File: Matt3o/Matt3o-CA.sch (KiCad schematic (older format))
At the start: 152 parts, among them IC1 ATMEGA32U4, K1 AVR_ICSP, P1 CONN_4, P2 CONN_4, SW1 TILDE, SW10 FN, SW11 2, SW12 W, SW13 S, SW14 X, SW15 ALT, SW16 3, SW17 E, SW18 D, SW19 C, SW2 TAB, SW20 4, SW21 R, SW22 F, SW23 V, SW24 5, SW25 T, SW26 G, SW27 B, SW28 SPACE, SW29 6, SW3 CAPS, SW30 Y, SW31 H, SW32 N, SW33 7, SW34 U, SW35 J, SW36 M, SW37 8, SW38 I, SW39 K, SW4 SHIFT, SW40 ,, SW41 9, SW42 O, SW43 L, SW44 ., SW45 ALT_R, SW46 0, SW47 P, SW48 ;, SW49 /, SW5 CTRL, SW50 CTRL_R, SW51 -, SW52 {, SW53 ', SW54 SHIFT_R, SW55 LEFT, SW56 =, SW57 }, SW58 ENTER, SW59 BCKSP, SW6 1, SW60 |, SW61 UP, SW62 DOWN, SW63 INS, SW64 DEL, SW65 PRINT, SW66 PAUSE, SW67 RIGHT, SW7 Q, SW8 A, SW9 Z, X1 ASX4

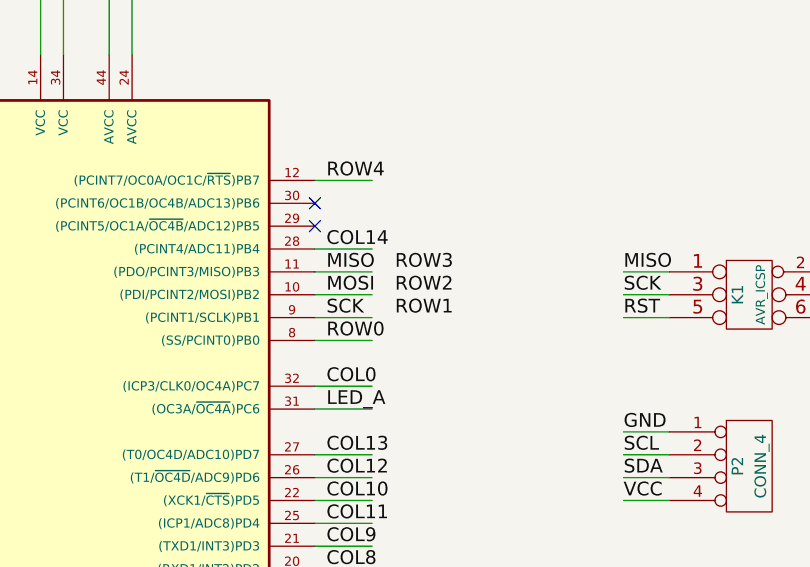
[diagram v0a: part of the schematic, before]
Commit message: review moving diodes out of switch area.
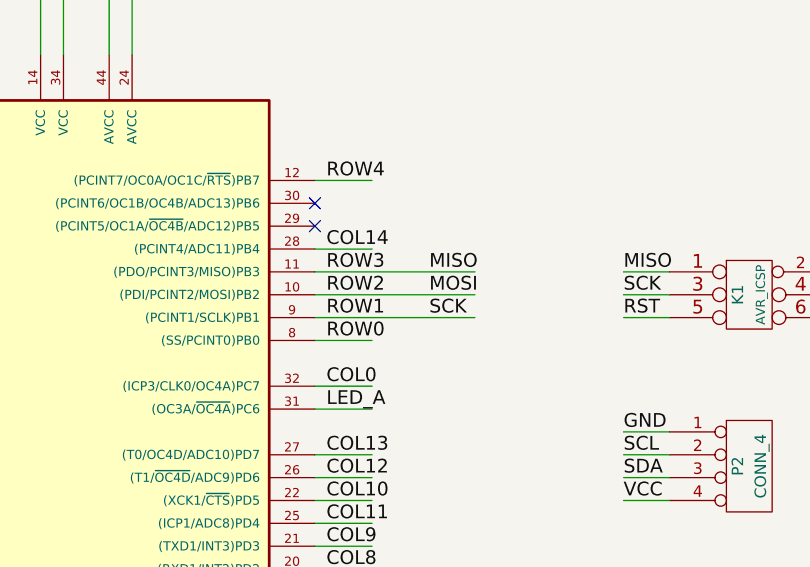
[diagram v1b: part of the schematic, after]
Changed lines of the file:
@@
-EESchema Schematic File Version 2  date 21/04/2013 16:00:32
+EESchema Schematic File Version 2  date 22/04/2013 01:50:13
 LIBS:components
 LIBS:Matt3o-CA-cache
@@
 Sheet 1 1
 Title ""
-Date "21 apr 2013"
+Date "22 apr 2013"
 Rev ""
 Comp ""
@@
 Wire Wire Line
 	2700 5400 2500 5400
-Wire Wire Line
-	6550 7550 6800 7550
-Wire Wire Line
-	6550 7650 6800 7650
-Wire Wire Line
-	6550 7750 6800 7750
-Text Label 6600 7550 0    60   ~ 0
+Text Label 7050 7550 0    60   ~ 0
 MISO
-Text Label 6600 7650 0    60   ~ 0
+Text Label 7050 7650 0    60   ~ 0
 MOSI
-Text Label 6600 7750 0    60   ~ 0
+Text Label 7050 7750 0    60   ~ 0
 SCK
 Text Label 7900 7550 0    60   ~ 0
@@
 Text Label 6600 7850 0    60   ~ 0
 ROW0
-Text Label 6900 7750 0    60   ~ 0
+Text Label 6600 7750 0    60   ~ 0
 ROW1
-Text Label 6900 7650 0    60   ~ 0
+Text Label 6600 7650 0    60   ~ 0
 ROW2
-Text Label 6900 7550 0    60   ~ 0
+Text Label 6600 7550 0    60   ~ 0
 ROW3
 Text Label 6600 7150 0    60   ~ 0
@@
 Text Label 6600 7450 0    60   ~ 0
 COL14
+Wire Wire Line
+	6550 7750 7250 7750
+Wire Wire Line
+	6550 7650 7250 7650
+Wire Wire Line
+	6550 7550 7250 7550
 $EndSCHEMATC

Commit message: final version touches.
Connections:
- net labels added: NU1, NU2
- wire segments 360 -> 362
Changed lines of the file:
@@
-EESchema Schematic File Version 2  date 22/04/2013 01:50:13
+EESchema Schematic File Version 2  date 24/04/2013 18:35:39
 LIBS:components
 LIBS:Matt3o-CA-cache
@@
 Sheet 1 1
 Title ""
-Date "22 apr 2013"
+Date "24 apr 2013"
 Rev ""
 Comp ""
@@
 	1    0    0    -1
 $EndComp
-NoConn ~ 6550 7250
-NoConn ~ 6550 7350
 $Comp
 L VCC #PWR02
@@
 Wire Wire Line
 	6550 7550 7250 7550
+Wire Wire Line
+	6550 7250 6800 7250
+Wire Wire Line
+	6550 7350 6800 7350
+Text Label 6600 7250 0    60   ~ 0
+NU1
+Text Label 6600 7350 0    60   ~ 0
+NU2
+NoConn ~ 6800 7250
+NoConn ~ 6800 7350
 $EndSCHEMATC
